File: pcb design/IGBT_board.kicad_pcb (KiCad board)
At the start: 6 copper layers, 150 x 100 mm, 170 parts, among them J1 4-794627-0, Q1 IGBT, Q10 IGBT, Q11 IGBT, Q12 IGBT, Q13 NPN, Q14 PNP, Q15 CSD19533Q5A, Q16 CSD19533Q5A, Q17 NPN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

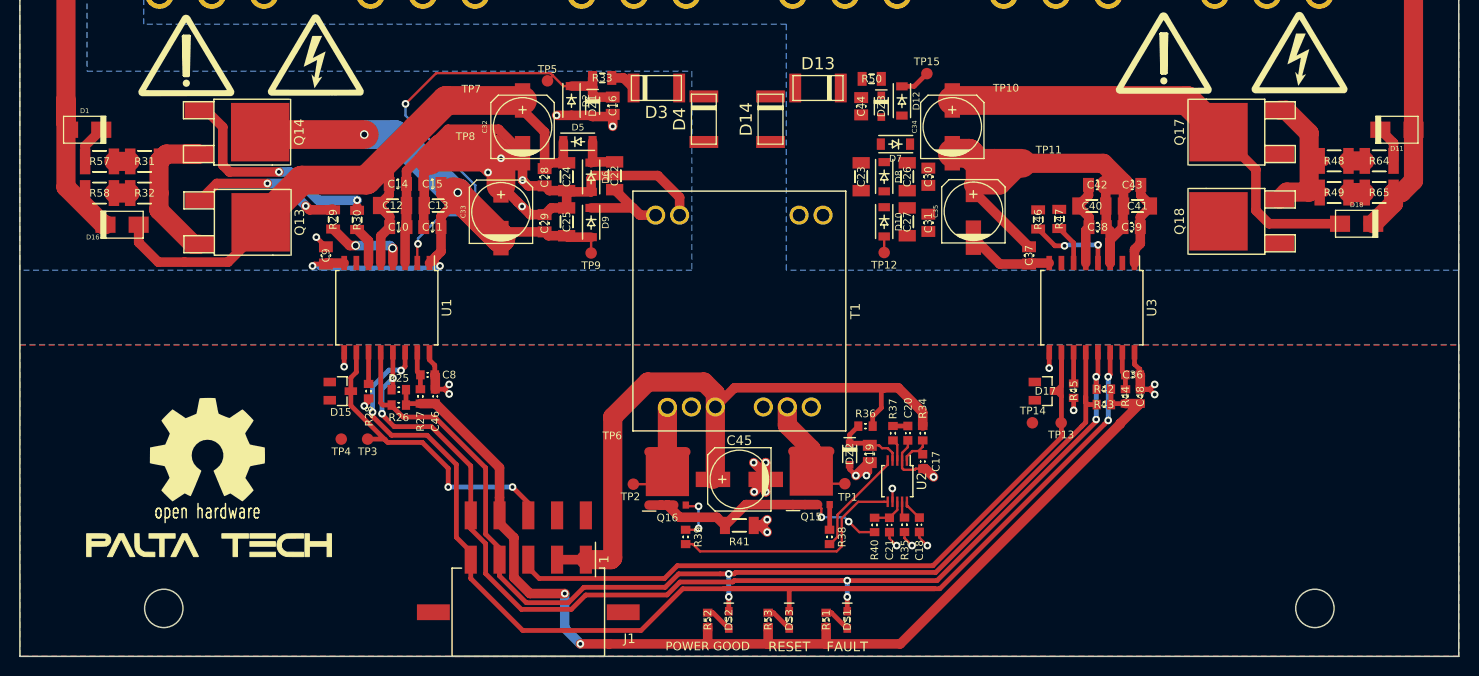
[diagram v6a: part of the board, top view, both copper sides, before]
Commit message: Changed GND copper plane to avoid coupling between phase output and controller GND (112pF->13pF)
Signed-off-by: Marcos Chaparro <mchaparro@paltatech.com>
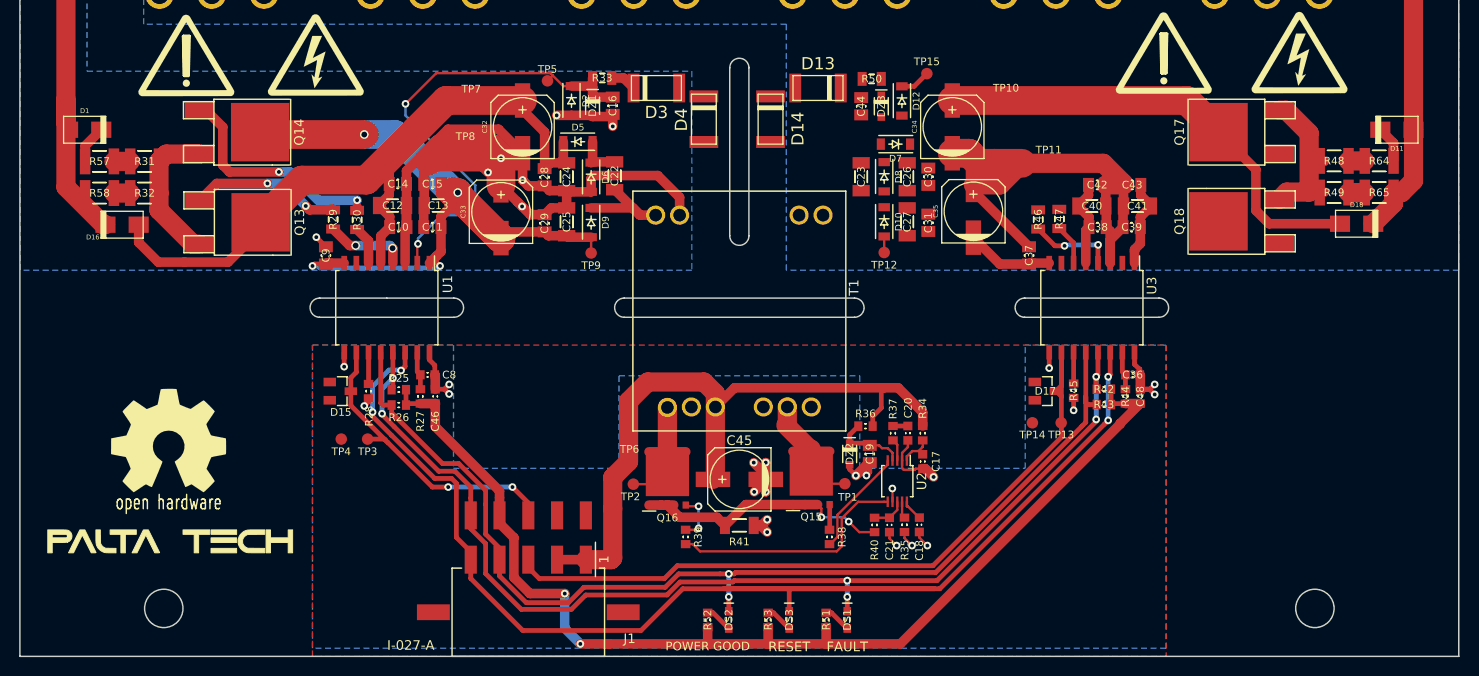
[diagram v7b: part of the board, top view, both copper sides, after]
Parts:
- moved G*** 4.16 mm to (-59.5, 27.5)
- moved G*** 4.07 mm to (-59.5, 38.0)
- moved TP6 2.28 mm to (-11.4, 29.6)
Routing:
- net /FAULT: track 116.7 -> 115.4 mm
- net /IN_TOP: track 32.8 -> 31.7 mm
- net /RESET: track 141.2 -> 140.1 mm
- net /READY: track 114.1 -> 113.2 mm
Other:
- outline, holes or cut-outs redrawn
- board text added: "Capacitive coumpling between bottom gnd and bottom-er phase copper plane is calculated this way: C=(4.7)(8.854×10−12)A(1.6×10−3) So, in this case with 1mm separator: (4.7*8.854*10^-12*0.09*0.03)/0.001 = 112pF"
- board text added: "I-027-A"

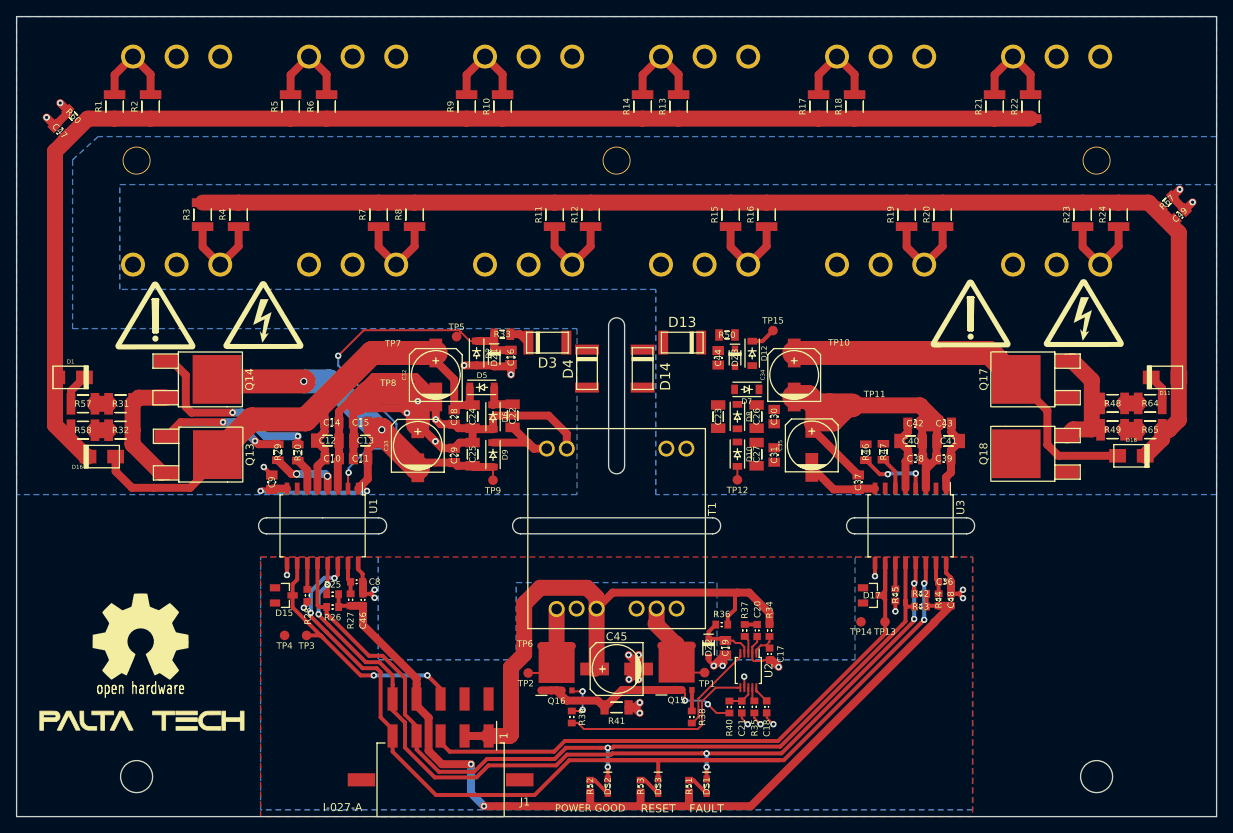
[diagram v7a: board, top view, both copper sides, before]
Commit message: Added board dimensions and improved gate return path
Signed-off-by: Marcos Chaparro <mchaparro@paltatech.com>
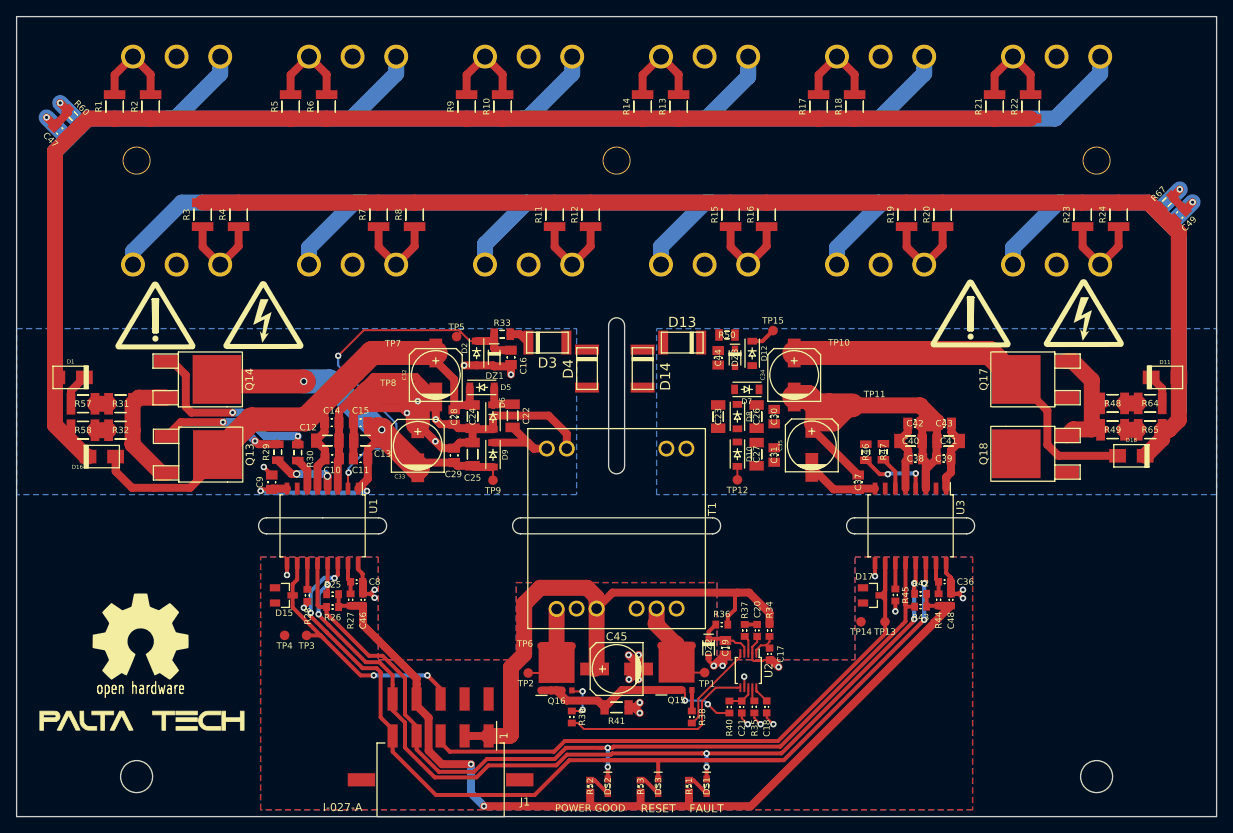
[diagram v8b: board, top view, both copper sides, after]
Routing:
- net PHASE: track 103.7 -> 333.6 mm
- net VBUS-: track 63.6 -> 283.5 mm
